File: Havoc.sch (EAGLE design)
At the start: 34 parts, among them T1 2N3904, T2 2N3904, T3 2N3904, T4 2N3904, T5 2N3904, T6 2N3904, U1 ATMEGA328P_PDIP, U2 FT231XS, Y1 16MHz

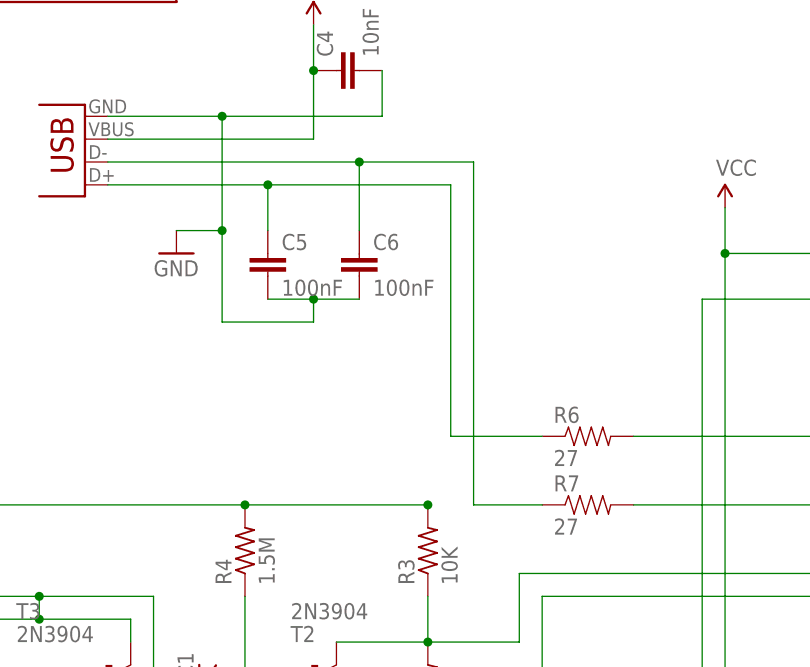
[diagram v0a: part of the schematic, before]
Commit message: Switch USBDP/USBDM.
When switching out USB parts, didn't catch the fact that D+ and
D- had switched positions as well.
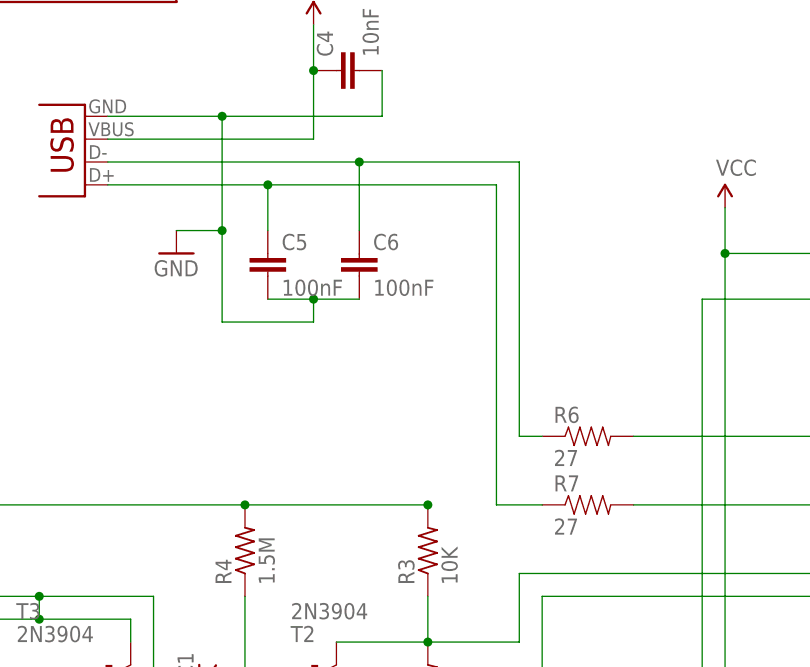
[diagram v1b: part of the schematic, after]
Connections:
- net N$13: now also R6.1; no longer R7.1
- net N$14: now also R7.1; no longer R6.1
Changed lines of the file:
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@@
 <wire x1="-15.24" y1="119.38" x2="-15.24" y2="124.46" width="0.1524" layer="91"/>
 <wire x1="-15.24" y1="124.46" x2="-33.02" y2="124.46" width="0.1524" layer="91"/>
-<wire x1="-15.24" y1="124.46" x2="5.08" y2="124.46" width="0.1524" layer="91"/>
-<pinref part="R6" gate="G$1" pin="1"/>
-<wire x1="5.08" y1="96.52" x2="15.24" y2="96.52" width="0.1524" layer="91"/>
-<wire x1="5.08" y1="124.46" x2="5.08" y2="96.52" width="0.1524" layer="91"/>
+<wire x1="-15.24" y1="124.46" x2="10.16" y2="124.46" width="0.1524" layer="91"/>
 <junction x="-15.24" y="124.46"/>
+<pinref part="R7" gate="G$1" pin="1"/>
+<wire x1="15.24" y1="88.9" x2="10.16" y2="88.9" width="0.1524" layer="91"/>
+<wire x1="10.16" y1="88.9" x2="10.16" y2="124.46" width="0.1524" layer="91"/>
 </segment>
 </net>
 <net name="N$13" class="0">
 <segment>
-<pinref part="R7" gate="G$1" pin="1"/>
-<wire x1="7.62" y1="88.9" x2="15.24" y2="88.9" width="0.1524" layer="91"/>
-<wire x1="7.62" y1="88.9" x2="7.62" y2="127" width="0.1524" layer="91"/>
 <pinref part="JP1" gate="G$1" pin="D-"/>
 <wire x1="-33.02" y1="127" x2="-5.08" y2="127" width="0.1524" layer="91"/>
 <pinref part="C6" gate="G$1" pin="1"/>
 <wire x1="-5.08" y1="119.38" x2="-5.08" y2="127" width="0.1524" layer="91"/>
-<wire x1="7.62" y1="127" x2="-5.08" y2="127" width="0.1524" layer="91"/>
+<wire x1="12.7" y1="127" x2="-5.08" y2="127" width="0.1524" layer="91"/>
 <junction x="-5.08" y="127"/>
+<pinref part="R6" gate="G$1" pin="1"/>
+<wire x1="15.24" y1="96.52" x2="12.7" y2="96.52" width="0.1524" layer="91"/>
+<wire x1="12.7" y1="96.52" x2="12.7" y2="127" width="0.1524" layer="91"/>
 </segment>
 </net>

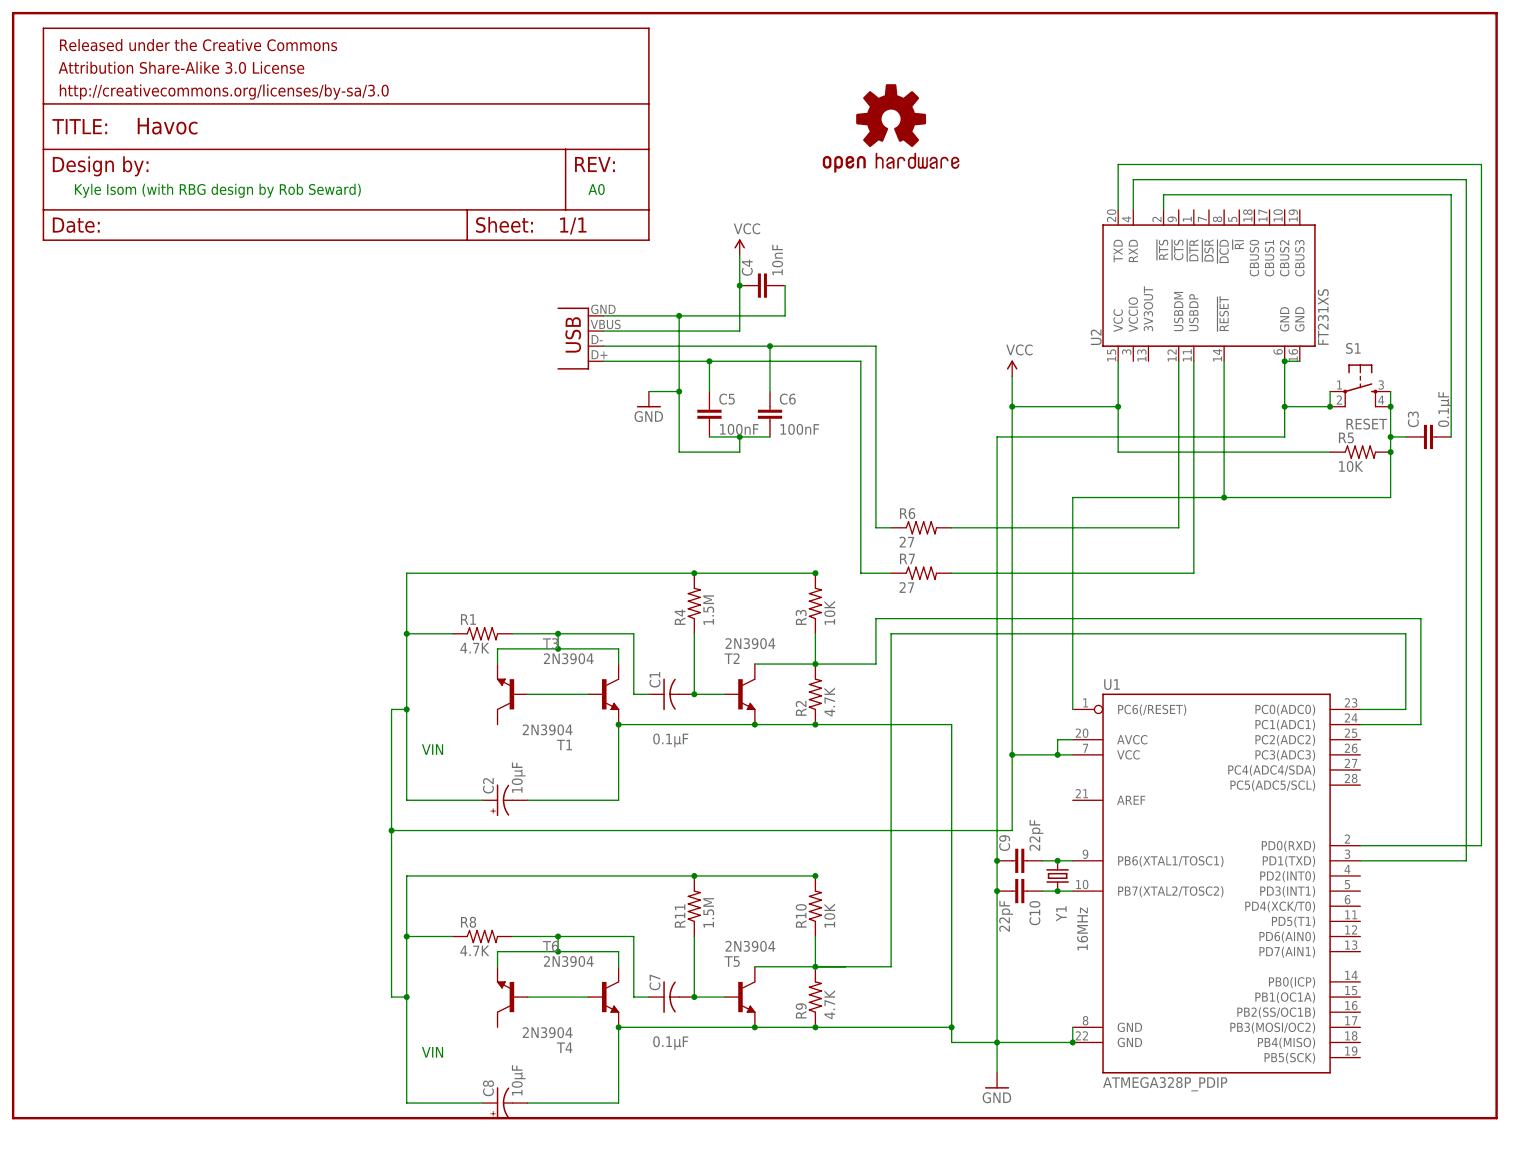
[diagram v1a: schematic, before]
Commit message: Add non-commercial part to license.
The upstream designs (Rob Seward's / Aaron Logue's) are both released
under a non-commercial license, and this must be respected.
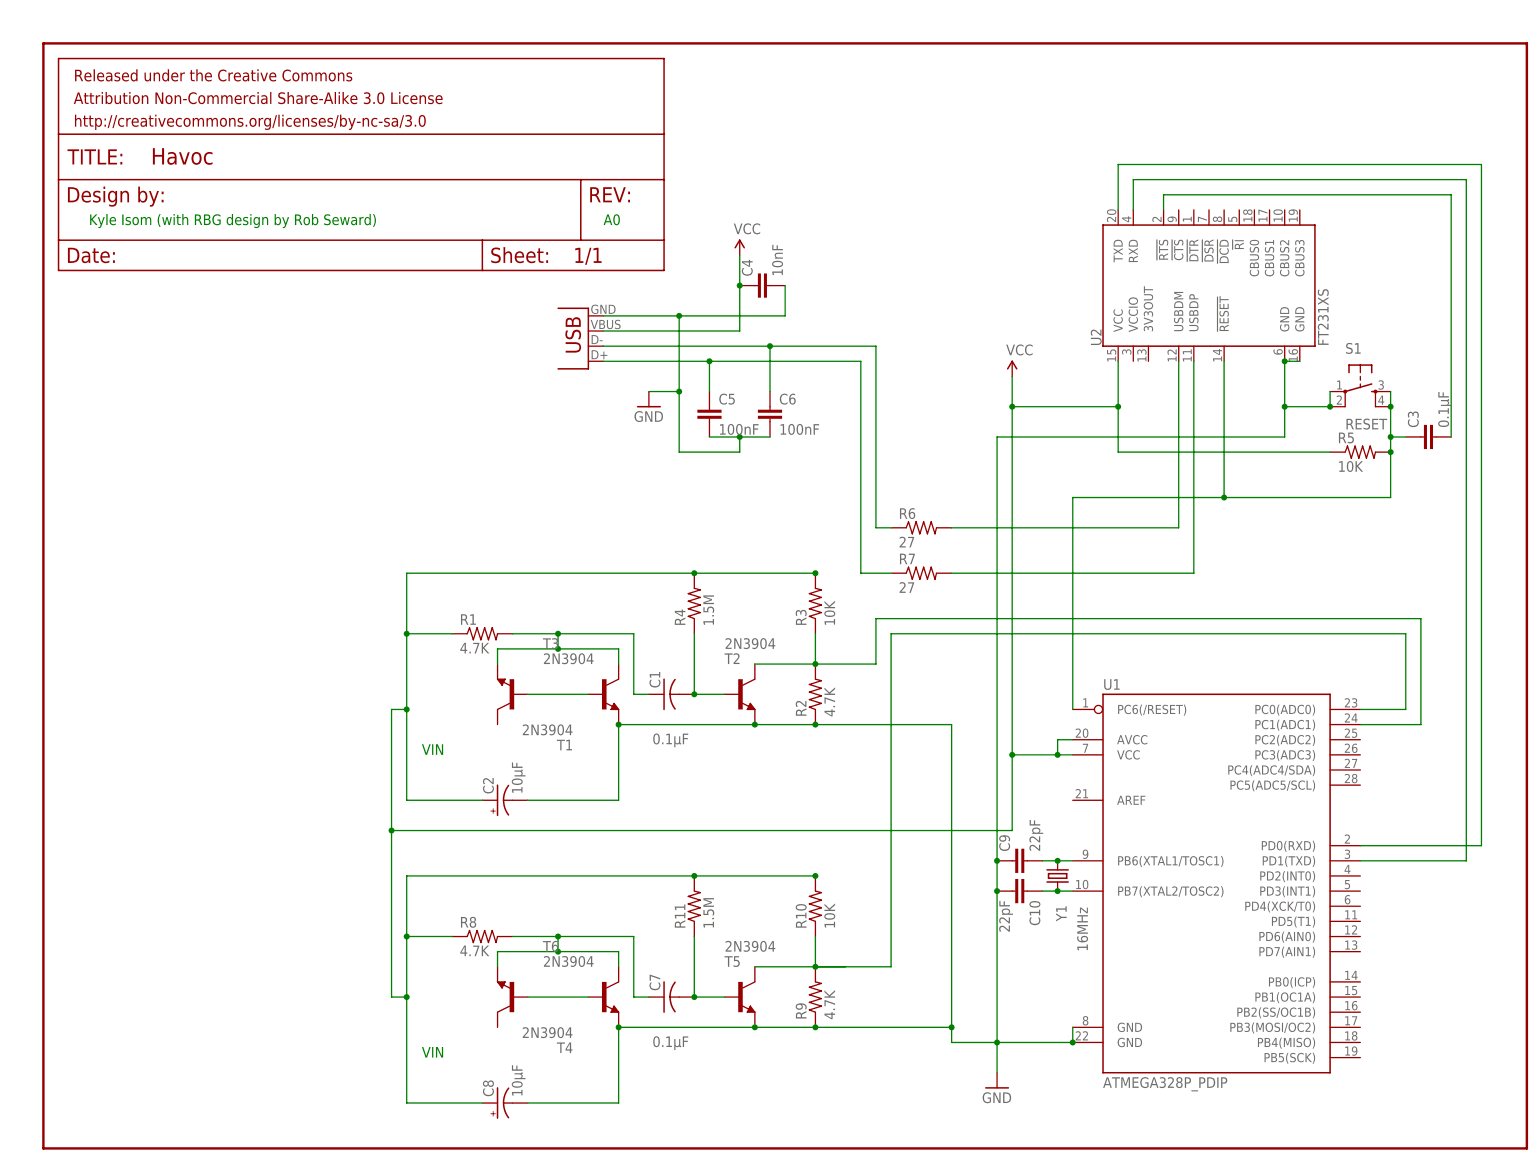
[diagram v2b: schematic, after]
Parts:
- removed LOGO1: OSHW-LOGOM, SparkFun-Aesthetics:OSHW-LOGOM
- FRAME1: device SparkFun-Aesthetics:FRAME-LETTER -> Aesthetics:FRAME-LETTER
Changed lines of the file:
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@@
 <layers>
 <layer number="1" name="Top" color="4" fill="1" visible="no" active="no"/>
+<layer number="2" name="Route2" color="1" fill="3" visible="no" active="no"/>
+<layer number="3" name="Route3" color="4" fill="3" visible="no" active="no"/>
+<layer number="14" name="Route14" color="1" fill="6" visible="no" active="no"/>
+<layer number="15" name="Route15" color="4" fill="6" visible="no" active="no"/>
 <layer number="16" name="Bottom" color="1" fill="1" visible="no" active="no"/>
 <layer number="17" name="Pads" color="2" fill="1" visible="no" active="no"/>
@@
 <part name="C7" library="resistor" deviceset="C-US" device="050-030X075" value="0.1µF"/>
 <part name="C8" library="resistor" deviceset="CPOL-US" device="E2-5" value="10µF"/>
-<part name="FRAME1" library="SparkFun-Aesthetics" deviceset="FRAME-LETTER" device=""/>
 <part name="Y1" library="SparkFun-FreqCtrl" deviceset="CRYSTAL" device="HC49US" value="16MHz"/>
 <part name="C9" library="SparkFun-Capacitors" deviceset="CAP" device="PTH" value="22pF"/>
 <part name="C10" library="SparkFun-Capacitors" deviceset="CAP" device="PTH" value="22pF"/>
-<part name="LOGO1" library="SparkFun-Aesthetics" deviceset="OSHW-LOGO" device="M"/>
+<part name="FRAME1" library="Aesthetics" deviceset="FRAME-LETTER" device=""/>
 </parts>
 <sheets>
@@
 <text x="-63.5" y="58.42" size="1.778" layer="91">VIN</text>
 <text x="-63.5" y="7.62" size="1.778" layer="91">VIN</text>
-<text x="-121.92" y="152.4" size="1.778" layer="91">Kyle Isom (with RBG design by Rob Seward)</text>
-<text x="-35.56" y="152.4" size="1.778" layer="91">A0</text>
+<text x="-119.38" y="147.32" size="1.778" layer="91">Kyle Isom (with RBG design by Rob Seward)</text>
+<text x="-33.02" y="147.32" size="1.778" layer="91">A0</text>
 </plain>
 <instances>
@@
 </instance>
 <instance part="C8" gate="G$1" x="-50.8" y="0" rot="R90"/>
-<instance part="FRAME1" gate="G$1" x="116.84" y="182.88" rot="R180"/>
-<instance part="FRAME1" gate="G$2" x="-127" y="144.78"/>
 <instance part="Y1" gate="G$1" x="43.18" y="38.1" smashed="yes" rot="R90">
 <attribute name="NAME" x="44.704" y="30.48" size="1.778" layer="95" rot="R90"/>
@@
 <instance part="C9" gate="G$1" x="38.1" y="40.64" rot="R90"/>
 <instance part="C10" gate="G$1" x="35.56" y="35.56" rot="R270"/>
-<instance part="LOGO1" gate="G$1" x="15.24" y="165.1"/>
+<instance part="FRAME1" gate="G$1" x="-127" y="-7.62" smashed="yes"/>
+<instance part="FRAME1" gate="G$2" x="-124.46" y="139.7"/>
 </instances>
 <busses>
@@
 </schematic>
 </drawing>
+<compatibility>
+<note version="6.3" minversion="6.2.2" severity="warning">
+Since Version 6.2.2 text objects can contain more than one line,
+which will not be processed correctly with this version.
+</note>
+</compatibility>
 </eagle>
